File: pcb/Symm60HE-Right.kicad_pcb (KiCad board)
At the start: 2 copper layers, 155.5 x 106.4 mm, 124 parts

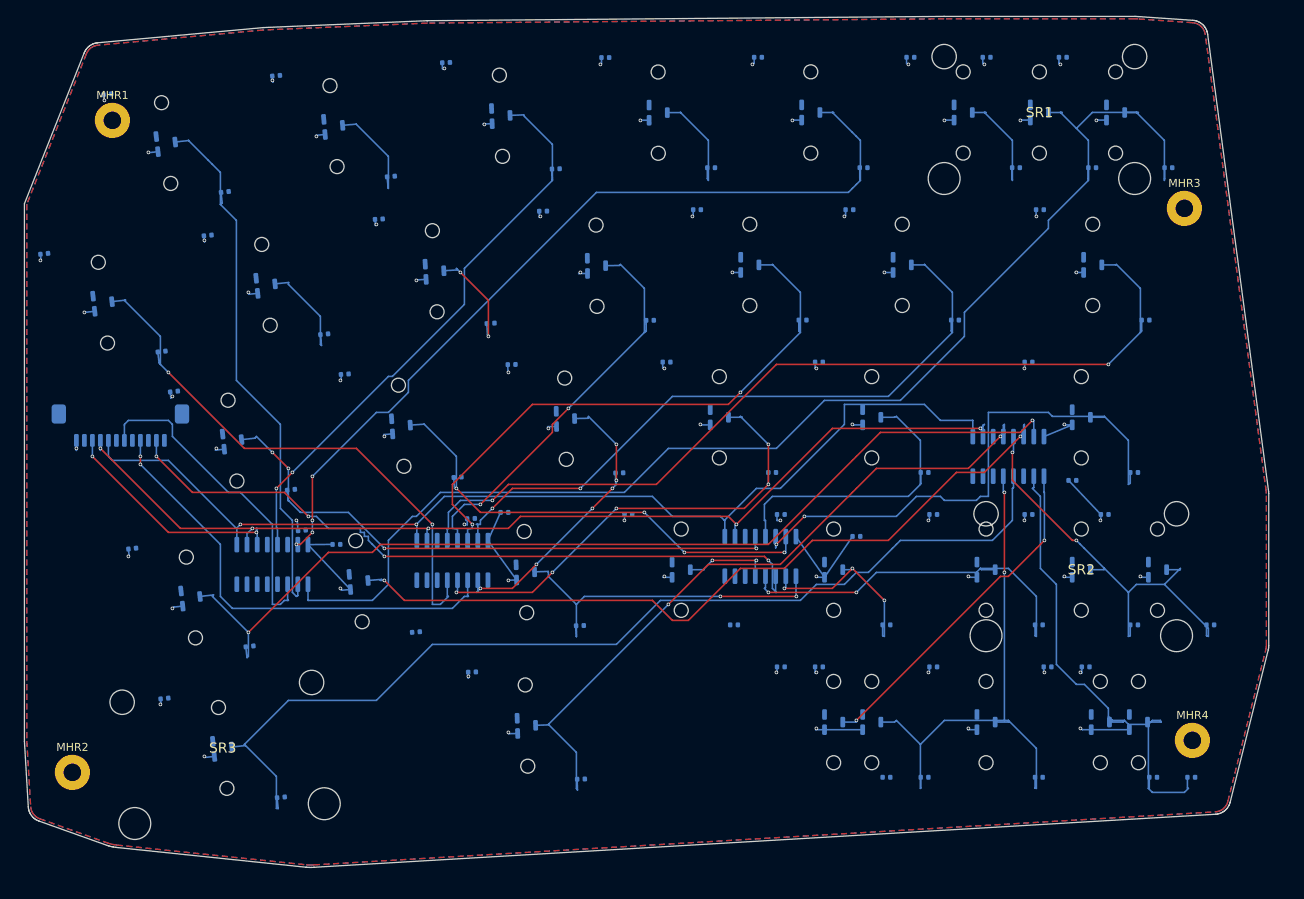
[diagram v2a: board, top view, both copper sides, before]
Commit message: Replace repo contents with current Symm60HE project folder
Adds firmware (libhmk), release fabrication outputs, pogo/neo PCB variants,
Fusion 360 case sources, and updated docs/tools.

Co-Authored-By: Claude Opus 5 <noreply@anthropic.com>
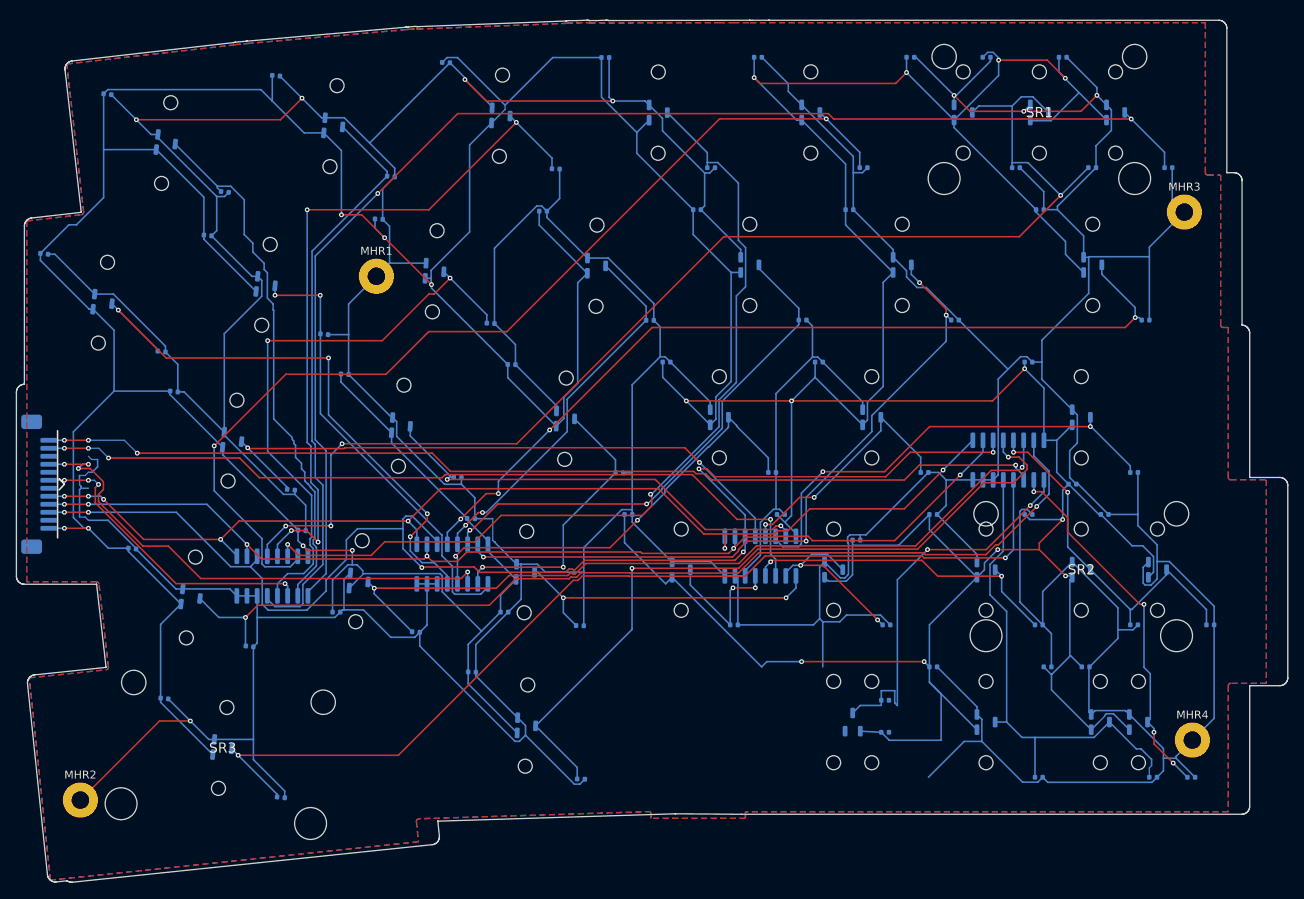
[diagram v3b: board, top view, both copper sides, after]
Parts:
- removed CR31A: 100n, Symm60HE_Project:C1_C_0402_1005Metric
- removed CR31B: 4.7n, Symm60HE_Project:C1_C_0402_1005Metric
- removed HER31: MT9102ET, Symm60HE_Project:HE_KEY_1.50u
- added KMR30A: MX_MECHANICAL_ONLY, HE_KEY_MECHANICAL_ONLY, B.Cu at (258.1, 85.7)
- added KMR30N: MX_MECHANICAL_ONLY, HE_KEY_MECHANICAL_ONLY, B.Cu at (253.4, 85.7)
- HER1, HER10, HER12, HER13, HER14, HER15, HER16, HER17, HER19, HER2, HER20, HER21, HER22, HER23, HER24, HER27, HER28, HER29, HER3, HER32, HER34, HER5, HER6, HER7, HER8, HER9: footprint Symm60HE_Project:HE_KEY_1.00u -> HE_KEY_1.00u
- HER11, HER33, HER35: footprint Symm60HE_Project:HE_KEY_1.50u -> HE_KEY_1.50u
- HER18: footprint Symm60HE_Project:HE_KEY_1.75u -> HE_KEY_1.75u
- HER25, HER36: footprint Symm60HE_Project:HE_KEY_2.25u -> HE_KEY_2.25u
- HER26: footprint Symm60HE_Project:HE_KEY_1.25u -> HE_KEY_1.25u
- HER30: footprint Symm60HE_Project:HE_KEY_1.00u -> HE_SHARED_MIDPOINT
- HER4: footprint Symm60HE_Project:HE_KEY_2.00u -> HE_KEY_2.00u
- moved MHR1 38.3 mm to (196.2, 30.0)
- moved CR30A 15.4 mm to (259.8, 87.0)
- moved JR1 12.5 mm to (154.2, 56.0), turned to 90 degrees
- moved CMR2 12.5 mm to (212.2, 72.0)
- moved CR30B 9.63 mm to (259.8, 83.0)
- moved CMR1 8.46 mm to (191.2, 72.0)
- moved MHR2 3.60 mm to (159.2, 95.5)
- moved HER30 2.38 mm to (255.7, 85.7), turned to 90 degrees
- moved AMR1 1.46 mm to (183.2, 67.5)
- moved AMR4 0.46 mm to (275.2, 53.0)
- moved CMR3 0.46 mm to (256.2, 63.0)
- moved CMR4 0.46 mm to (283.2, 56.0)
- moved MHR3 0.46 mm to (297.2, 22.0)
- moved AMR2 0.46 mm to (205.7, 66.0)
- turned CR22A to -0.03 degrees
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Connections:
- CR33B pad 1: HE_R31 -> HE_R30
- CR4B pad 1: HE_R05 -> HE_R04
- HER33 pad 3: HE_R31 -> HE_R30
- HER4 pad 3: HE_R05 -> HE_R04
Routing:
- net GND: track 0.00 -> 1151.2 mm, vias 0 -> 8
- net +3V3A: track 131.4 -> 957.1 mm, vias 71 -> 19
- net HE_R04: track 13.5 -> 155.4 mm, vias 0 -> 4
- net MUX_A0: track 29.1 -> 166.1 mm, vias 2 -> 6
- net ADC_R4: track 0.00 -> 125.0 mm, vias 0 -> 4
- net HE_R02: track 13.4 -> 109.8 mm, vias 0 -> 2
- net HE_R06: track 12.9 -> 72.8 mm
- net HE_R08: track 13.7 -> 72.1 mm
- net HE_R13: track 12.7 -> 56.1 mm, vias 0 -> 2
- net HE_R03: track 107.9 -> 125.0 mm, vias 4 -> 2
- net HE_R01: track 73.0 -> 89.4 mm, vias 2 -> 4
- net HE_R31: track 62.1 -> 46.3 mm, vias 0 -> 4
- net HE_R18: track 69.7 -> 59.1 mm
- net ADC_R3: track 91.3 -> 100.6 mm
- net HE_R25: track 55.0 -> 46.1 mm
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- added copper zone on F.Cu, net GND
- removed copper zone on F.Cu, net +3V3A
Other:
- board size 155.5 x 106.4 mm -> 158.9 x 107.8 mm

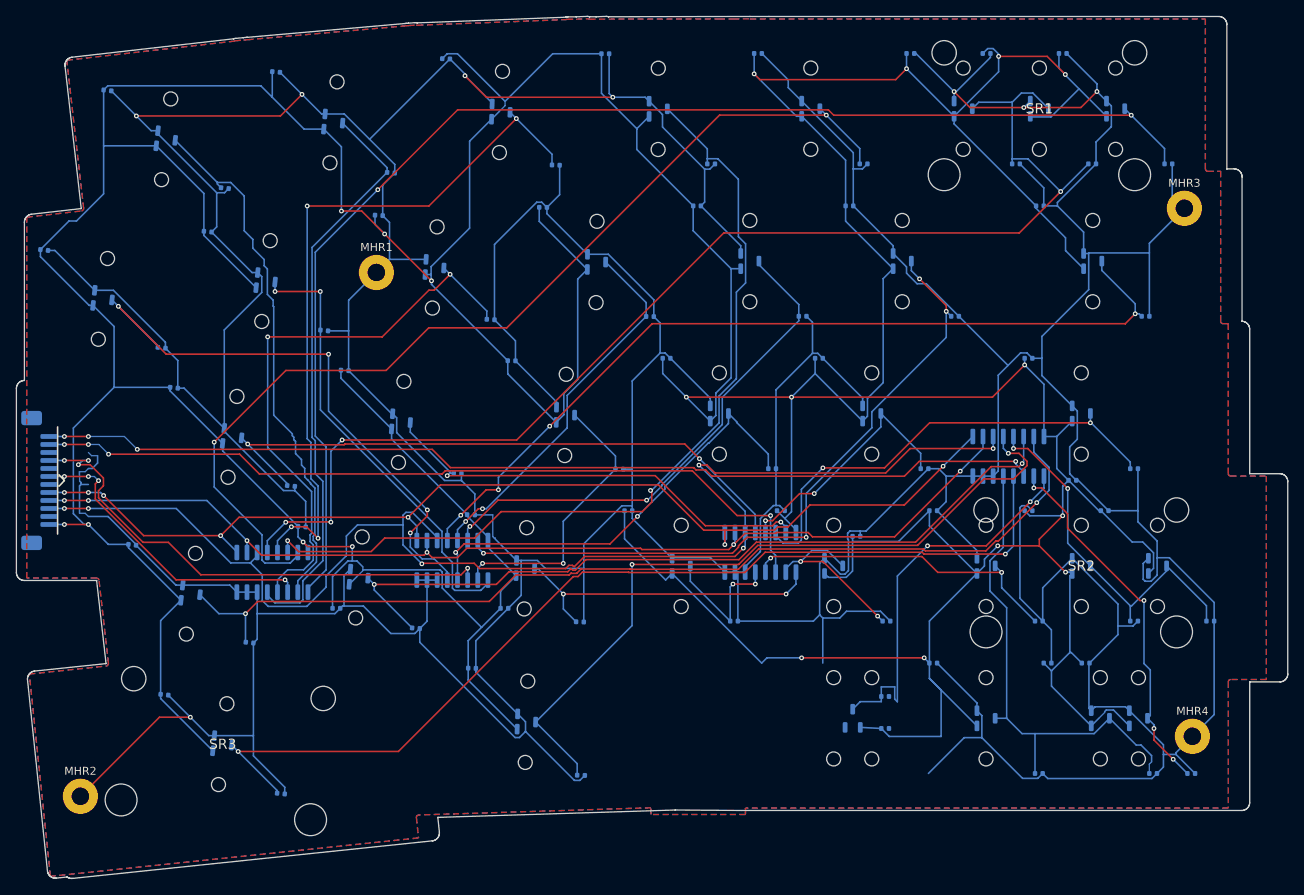
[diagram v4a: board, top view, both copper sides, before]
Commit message: Replace the project with the reorganised T7 tree: ribbon keyboard is production, pogo archived
Production design is now the outward-facing FPC keyboard with per-key
SK6812MINI-E reverse-mount LEDs, a fifth SN74LV4051A mux per half so every
alternate Hall position has its own channel, an SN74AHCT1G125 LED level
shifter, a 50 x 31 mm daughterboard, 1.5 mm POM plates and 3 degree / 7 degree
tent and typing angles. The universal half panel is fully populated (359
placements) with routed NPTH alignment slots for the mutually exclusive
positions, and eight fixed-layout Left/Right PCB pairs are released under
release/layout-pcbs/ with matching BOM, CPL, Gerber ZIP, drill report and DRC.

Reorganise tools/ into cad/, generators/, layouts/, pcb/, pogo/, releases/ and
rendering/ subpackages; add designs/ and layout/ (KLE) trees and per-layout
gallery renders. The Fusion handoff is a fourteen-body reference STEP with
Gateron KS-20 switch and Cherry-profile keycap references and exact BOOMELE,
HRO and XKB models under case/fusion360/models/official/ with provenance.

The Neo-style pogo variant, its Mill-Max vendor models, the Fusion setup
script and the pogo release packages are archived as design history and
marked DO-NOT-ORDER. Their restored BOM snapshots had reintroduced the wrong
mux part C7792; corrected to C128414 / SN74LV4051ADR and their checksum lists
and archives rebuilt.

Co-Authored-By: Claude Opus 5 <noreply@anthropic.com>
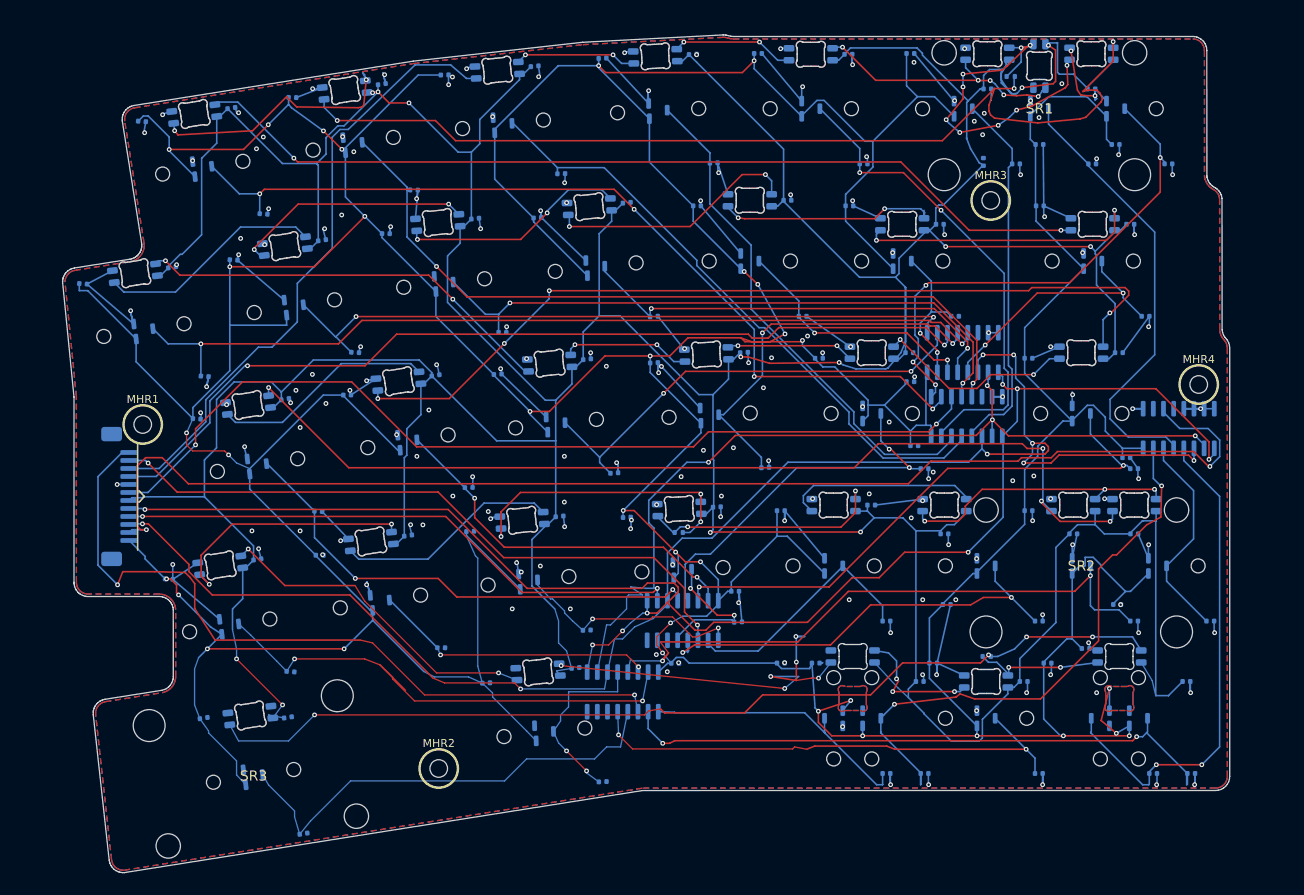
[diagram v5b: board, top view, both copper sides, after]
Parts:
- removed KMR30A, KMR30N: MX_MECHANICAL_ONLY, HE_KEY_MECHANICAL_ONLY
- added AMR5: SN74LV4051A, Symm60HE_Project:AM1_SOIC-16_3.9x9.9mm_P1.27mm, B.Cu at (296.5, 49.5)
- added CMR5: 100n, Symm60HE_Project:C1_C_0402_1005Metric, B.Cu at (289.9, 53.1)
- added CR31A: 100n, Symm60HE_Project:C1_C_0402_1005Metric, B.Cu at (251.1, 78.8)
- added CR31B: 4.7n, Symm60HE_Project:C1_C_0402_1005Metric, B.Cu at (264.7, 92.6)
- added CRGBR1: 100n, Symm60HE_Project:C1_C_0402_1005Metric, B.Cu at (216.0, 4.22)
- added CRGBR10: 100n, Symm60HE_Project:C1_C_0402_1005Metric, B.Cu at (247.6, 21.0)
- added CRGBR11: 100n, Symm60HE_Project:C1_C_0402_1005Metric, B.Cu at (227.5, 21.3)
- added CRGBR12: 100n, Symm60HE_Project:C1_C_0402_1005Metric, B.Cu at (208.6, 23.3)
- added CRGBR13: 100n, Symm60HE_Project:C1_C_0402_1005Metric, B.Cu at (189.4, 26.0)
- added CRGBR14: 100n, Symm60HE_Project:C1_C_0402_1005Metric, B.Cu at (170.7, 29.4)
- added CRGBR15: 100n, Symm60HE_Project:C1_C_0402_1005Metric, B.Cu at (222.5, 40.8)
- added CRGBR16: 100n, Symm60HE_Project:C1_C_0402_1005Metric, B.Cu at (242.2, 40.0)
- added CRGBR17: 100n, Symm60HE_Project:C1_C_0402_1005Metric, B.Cu at (262.8, 40.0)
- added CRGBR18: 100n, Symm60HE_Project:C1_C_0402_1005Metric, B.Cu at (289.0, 40.0)
- added CRGBR19: 100n, Symm60HE_Project:C1_C_0402_1005Metric, B.Cu at (203.6, 42.9)
- added CRGBR2: 100n, Symm60HE_Project:C1_C_0402_1005Metric, B.Cu at (235.8, 2.73)
- added CRGBR20: 100n, Symm60HE_Project:C1_C_0402_1005Metric, B.Cu at (184.8, 45.8)
- added CRGBR21: 100n, Symm60HE_Project:C1_C_0402_1005Metric, B.Cu at (283.3, 62.7)
- added CRGBR22: 100n, Symm60HE_Project:C1_C_0402_1005Metric, B.Cu at (267.2, 62.7)
- added CRGBR23: 100n, Symm60HE_Project:C1_C_0402_1005Metric, B.Cu at (258.1, 59.1)
- added CRGBR24: 100n, Symm60HE_Project:C1_C_0402_1005Metric, B.Cu at (238.8, 59.3)
- added CRGBR25: 100n, Symm60HE_Project:C1_C_0402_1005Metric, B.Cu at (219.1, 60.5)
- added CRGBR26: 100n, Symm60HE_Project:C1_C_0402_1005Metric, B.Cu at (200.2, 62.9)
- added CRGBR27: 100n, Symm60HE_Project:C1_C_0402_1005Metric, B.Cu at (181.3, 65.9)
- added CRGBR28: 100n, Symm60HE_Project:C1_C_0402_1005Metric, B.Cu at (221.1, 79.4)
- added CRGBR29: 100n, Symm60HE_Project:C1_C_0402_1005Metric, B.Cu at (264.1, 81.1)
- added CRGBR3: 100n, Symm60HE_Project:C1_C_0402_1005Metric, B.Cu at (255.2, 2.73)
- added CRGBR31: 100n, Symm60HE_Project:C1_C_0402_1005Metric, B.Cu at (297.5, 81.1)
- added CRGBR32: 100n, Symm60HE_Project:C1_C_0402_1005Metric, B.Cu at (185.1, 85.6)
- added CRGBR33: 100n, Symm60HE_Project:C1_C_0402_1005Metric, B.Cu at (272.1, 16.2)
- added CRGBR34: 100n, Symm60HE_Project:C1_C_0402_1005Metric, B.Cu at (290.9, 62.7)
- added CRGBR36: 100n, Symm60HE_Project:C1_C_0402_1005Metric, B.Cu at (277.1, 81.1)
- added CRGBR4: 100n, Symm60HE_Project:C1_C_0402_1005Metric, B.Cu at (272.6, 7.06)
- added CRGBR5: 100n, Symm60HE_Project:C1_C_0402_1005Metric, B.Cu at (285.6, 7.06)
- added CRGBR6: 100n, Symm60HE_Project:C1_C_0402_1005Metric, B.Cu at (196.9, 6.46)
- added CRGBR7: 100n, Symm60HE_Project:C1_C_0402_1005Metric, B.Cu at (178.1, 9.45)
- added CRGBR8: 100n, Symm60HE_Project:C1_C_0402_1005Metric, B.Cu at (290.4, 24.0)
- added CRGBR9: 100n, Symm60HE_Project:C1_C_0402_1005Metric, B.Cu at (266.6, 24.0)
- added DR1: SK6812MINI-E, Symm60HE_Project:SK6812MINI-E_ReverseMount, B.Cu at (211.3, 4.71)
- added DR10: SK6812MINI-E, Symm60HE_Project:SK6812MINI-E_ReverseMount, B.Cu at (242.9, 21.0)
- added DR11: SK6812MINI-E, Symm60HE_Project:SK6812MINI-E_ReverseMount, B.Cu at (222.8, 21.8)
- added DR12: SK6812MINI-E, Symm60HE_Project:SK6812MINI-E_ReverseMount, B.Cu at (203.9, 23.8)
- added DR13: SK6812MINI-E, Symm60HE_Project:SK6812MINI-E_ReverseMount, B.Cu at (184.8, 26.7)
- added DR14: SK6812MINI-E, Symm60HE_Project:SK6812MINI-E_ReverseMount, B.Cu at (166.0, 30.1)
- added DR15: SK6812MINI-E, Symm60HE_Project:SK6812MINI-E_ReverseMount, B.Cu at (217.9, 41.3)
- added DR16: SK6812MINI-E, Symm60HE_Project:SK6812MINI-E_ReverseMount, B.Cu at (237.5, 40.2)
- added DR17: SK6812MINI-E, Symm60HE_Project:SK6812MINI-E_ReverseMount, B.Cu at (258.1, 40.0)
- added DR18: SK6812MINI-E, Symm60HE_Project:SK6812MINI-E_ReverseMount, B.Cu at (284.3, 40.0)
- added DR19: SK6812MINI-E, Symm60HE_Project:SK6812MINI-E_ReverseMount, B.Cu at (199.0, 43.6)
- added DR2: SK6812MINI-E, Symm60HE_Project:SK6812MINI-E_ReverseMount, B.Cu at (231.1, 2.98)
- added DR20: SK6812MINI-E, Symm60HE_Project:SK6812MINI-E_ReverseMount, B.Cu at (180.2, 46.6)
- added DR21: SK6812MINI-E, Symm60HE_Project:SK6812MINI-E_ReverseMount, B.Cu at (283.3, 59.1)
- added DR22: SK6812MINI-E, Symm60HE_Project:SK6812MINI-E_ReverseMount, B.Cu at (267.2, 59.1)
- added DR23: SK6812MINI-E, Symm60HE_Project:SK6812MINI-E_ReverseMount, B.Cu at (253.4, 59.1)
- added DR24: SK6812MINI-E, Symm60HE_Project:SK6812MINI-E_ReverseMount, B.Cu at (234.1, 59.6)
- added DR25: SK6812MINI-E, Symm60HE_Project:SK6812MINI-E_ReverseMount, B.Cu at (214.4, 61.0)
- added DR26: SK6812MINI-E, Symm60HE_Project:SK6812MINI-E_ReverseMount, B.Cu at (195.5, 63.6)
- added DR27: SK6812MINI-E, Symm60HE_Project:SK6812MINI-E_ReverseMount, B.Cu at (176.7, 66.6)
- added DR28: SK6812MINI-E, Symm60HE_Project:SK6812MINI-E_ReverseMount, B.Cu at (216.4, 79.9)
- added DR29: SK6812MINI-E, Symm60HE_Project:SK6812MINI-E_ReverseMount, B.Cu at (255.7, 78.0)
- added DR3: SK6812MINI-E, Symm60HE_Project:SK6812MINI-E_ReverseMount, B.Cu at (250.5, 2.73)
- added DR31: SK6812MINI-E, Symm60HE_Project:SK6812MINI-E_ReverseMount, B.Cu at (289.1, 78.0)
- added DR32: SK6812MINI-E, Symm60HE_Project:SK6812MINI-E_ReverseMount, B.Cu at (180.5, 85.4)
- added DR33: SK6812MINI-E, Symm60HE_Project:SK6812MINI-E_ReverseMount, B.Cu at (279.1, 4.17)
- added DR34: SK6812MINI-E, Symm60HE_Project:SK6812MINI-E_ReverseMount, B.Cu at (290.9, 59.1)
- added DR36: SK6812MINI-E, Symm60HE_Project:SK6812MINI-E_ReverseMount, B.Cu at (272.4, 81.1)
- added DR4: SK6812MINI-E, Symm60HE_Project:SK6812MINI-E_ReverseMount, B.Cu at (272.6, 2.66)
- added DR5: SK6812MINI-E, Symm60HE_Project:SK6812MINI-E_ReverseMount, B.Cu at (285.6, 2.66)
- added DR6: SK6812MINI-E, Symm60HE_Project:SK6812MINI-E_ReverseMount, B.Cu at (192.2, 7.19)
- added DR7: SK6812MINI-E, Symm60HE_Project:SK6812MINI-E_ReverseMount, B.Cu at (173.4, 10.2)
- added DR8: SK6812MINI-E, Symm60HE_Project:SK6812MINI-E_ReverseMount, B.Cu at (285.8, 24.0)
- added DR9: SK6812MINI-E, Symm60HE_Project:SK6812MINI-E_ReverseMount, B.Cu at (261.9, 24.0)
- added HER31: MT9102ET, HE_KEY_1.50u, B.Cu at (258.1, 85.7)
- added RBPR24: 0R_DNP, Symm60HE_Project:R3_R_0402_1005Metric, B.Cu at (234.0, 62.5)
- added RBPR31: 0R_DNP, Symm60HE_Project:R3_R_0402_1005Metric, B.Cu at (272.5, 78.0)
- added RBPR5: 0R_DNP, Symm60HE_Project:R3_R_0402_1005Metric, B.Cu at (275.5, 5.50)
- HER30: footprint HE_SHARED_MIDPOINT -> HE_KEY_1.00u
- MHR1, MHR2, MHR3, MHR4: value M2 -> M2_NPTH; footprint Symm60HE_Project:MountingHole_2.2mm_M2_Pad -> Symm60HE_Project:MountingHole_2.2mm_M2_NPTH
- moved AMR1 88.9 mm to (270.0, 48.0), turned to -90 degrees
- moved CMR1 75.0 mm to (263.4, 51.6)
- moved AMR2 68.9 mm to (269.5, 40.0), turned to -90 degrees
- moved CMR2 58.1 mm to (262.9, 43.6)
- moved AMR4 56.5 mm to (227.0, 82.4)
- moved CMR4 54.7 mm to (233.6, 78.9)
- moved MHR2 44.9 mm to (204.0, 92.0)
- moved MHR4 44.0 mm to (299.0, 44.0)
- moved MHR1 34.8 mm to (167.0, 49.0)
- moved MHR3 24.2 mm to (273.0, 21.0)
- moved CMR3 16.6 mm to (241.1, 69.9)
- moved CR30A 15.4 mm to (246.8, 78.8)
- moved CR4A 13.2 mm to (279.1, 14.0)
- moved CR5A 13.2 mm to (288.6, 14.0)
- moved AMR3 12.9 mm to (234.5, 73.5)
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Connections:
- CR26B pad 1: HE_R25 -> HE_R34
- CR33B pad 1: HE_R30 -> HE_R36
- CR4B pad 1: HE_R04 -> HE_R33
- HER26 pad 3: HE_R25 -> HE_R34
- HER33 pad 3: HE_R30 -> HE_R36
- HER4 pad 3: HE_R04 -> HE_R33
- JR1 pad 10: GND -> RGB_R
- JR1 pad 2: GND -> ADC_R5
- JR1 pad 6: GND -> VBUS
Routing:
- net GND: track 1151.2 -> 361.1 mm, vias 8 -> 177
- net VBUS: track 0.00 -> 757.4 mm, vias 0 -> 13
- net ADC_R5: track 0.00 -> 162.2 mm, vias 0 -> 2
- net RGB_R_05: track 0.00 -> 123.6 mm, vias 0 -> 3
- net RGB_R_20: track 0.00 -> 123.0 mm, vias 0 -> 4
- net RGB_R_31: track 0.00 -> 121.7 mm, vias 0 -> 4
- net RGB_R_07: track 0.00 -> 113.8 mm, vias 0 -> 2
- net RGB_R_18: track 0.00 -> 109.7 mm, vias 0 -> 4
- net HE_R04: track 155.4 -> 46.5 mm, vias 4 -> 0
- net HE_R05: track 162.6 -> 63.7 mm, vias 2 -> 4
- net ADC_R1: track 37.5 -> 116.5 mm, vias 4 -> 2
- net RGB_R: track 0.00 -> 77.4 mm
- net HE_R12: track 108.8 -> 33.2 mm, vias 4 -> 2
- net HE_R35: track 0.00 -> 71.4 mm, vias 0 -> 2
- net HE_R28: track 93.6 -> 22.9 mm
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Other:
- board size 158.9 x 107.8 mm -> 145.9 x 104.7 mm
